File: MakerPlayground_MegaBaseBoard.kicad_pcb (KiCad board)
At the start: 2 copper layers, 45 x 90 mm, 66 parts, among them J1 BattCon, J10 D5, J11 D6, J12 I2C, J13 I2C, J14 D1/A4, J15 D2/A5, J16 I2C, J2 ESP32, J3 USB, J4 Micro_SD_Card, J5 A1, J6 A2, J7 A3, J8 D3, J9 D4, Q1 Q_NPN_BEC, Q2 Q_NPN_BEC, SW1 Reset, U1 MCP73871, U2 TPS63001, U3 CP2102N-A01-GQFN24, U4 TXB0108DQSR

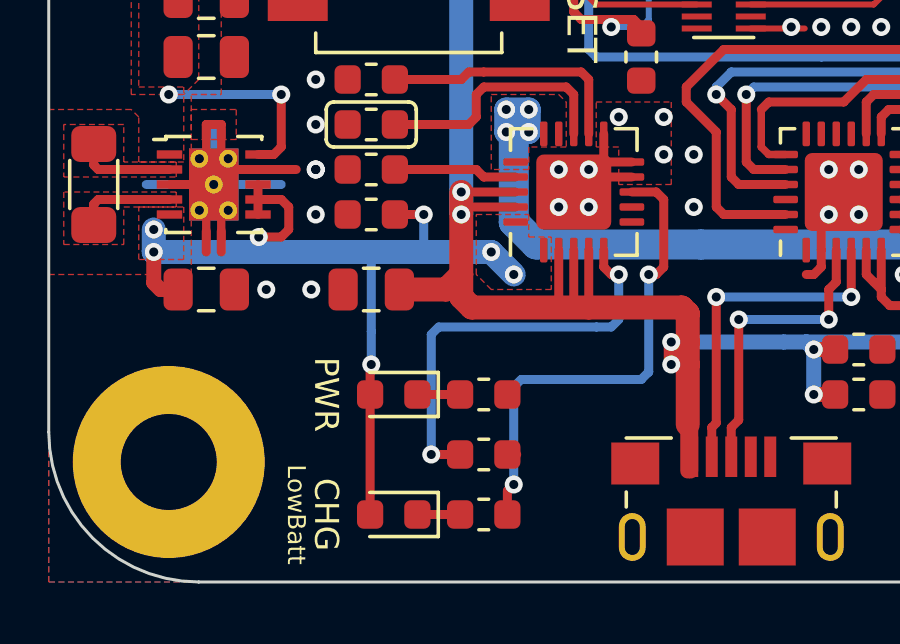
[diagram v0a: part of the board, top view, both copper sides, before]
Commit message: Add ON/OFF switch & new alignment for PWR/CHG LED.
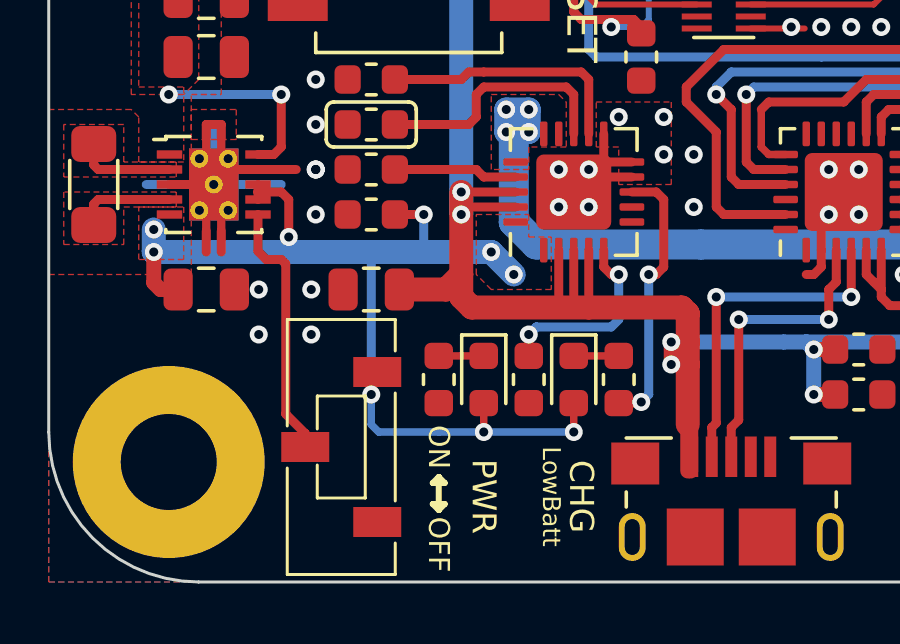
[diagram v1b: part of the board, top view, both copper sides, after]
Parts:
- added SW2: SW_SPDT, GiraffeTech-Electromechanical:SW_SPDT_CK-JS102011JCQN, F.Cu at (144.8, 150.5)
- moved D2 7.50 mm to (152.5, 148.2), turned to 270 degrees
- moved R10 6.36 mm to (154.0, 148.2), turned to 270 degrees
- moved D1 3.04 mm to (149.5, 148.2), turned to 270 degrees
- moved R1 2.92 mm to (151.0, 148.2), turned to 90 degrees
- moved R8 1.58 mm to (148.0, 148.2), turned to 270 degrees
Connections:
- REF** pad 1: (no net) -> GND (x4)
- U2 pad 6: VDD -> REG_EN
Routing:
- net REG_EN: track 0.00 -> 8.70 mm
- net Net-(R1-Pad2): track 14.1 -> 6.59 mm
- net LBO: track 16.3 -> 9.14 mm
- net VDD: track 30.6 -> 36.0 mm, vias 7 -> 9
- net GND: track 24.7 -> 24.4 mm, vias 74 -> 76
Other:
- board text added: "OFF"
- board text added: "ON"
